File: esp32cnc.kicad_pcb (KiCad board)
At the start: 2 copper layers, 88.3 x 113.7 mm, 25 parts, among them J1 Barrel_Jack, J2 USB_B_Micro, J3 Micro_SD_Card_Det1, J4 Screw_Terminal_01x04, J5 Screw_Terminal_01x04, J6 Screw_Terminal_01x04, J7 Screw_Terminal_01x02, U1 ESP32-WROOM-32, U2 OKI-78SR-3.3_1.5-W36-C, U3 CH330N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

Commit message: Init
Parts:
- moved J1 0.71 mm to (121.9, 122.9)
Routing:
- net unconnected-(J2-Shield-Pad6)_4: track 0.00 -> 16.3 mm
- net GND: track 63.1 -> 74.9 mm, vias 8 -> 9
- net +3.3V: track 173.7 -> 181.3 mm, vias 4 -> 8
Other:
- board size 88.3 x 113.7 mm -> 91.4 x 116.8 mm

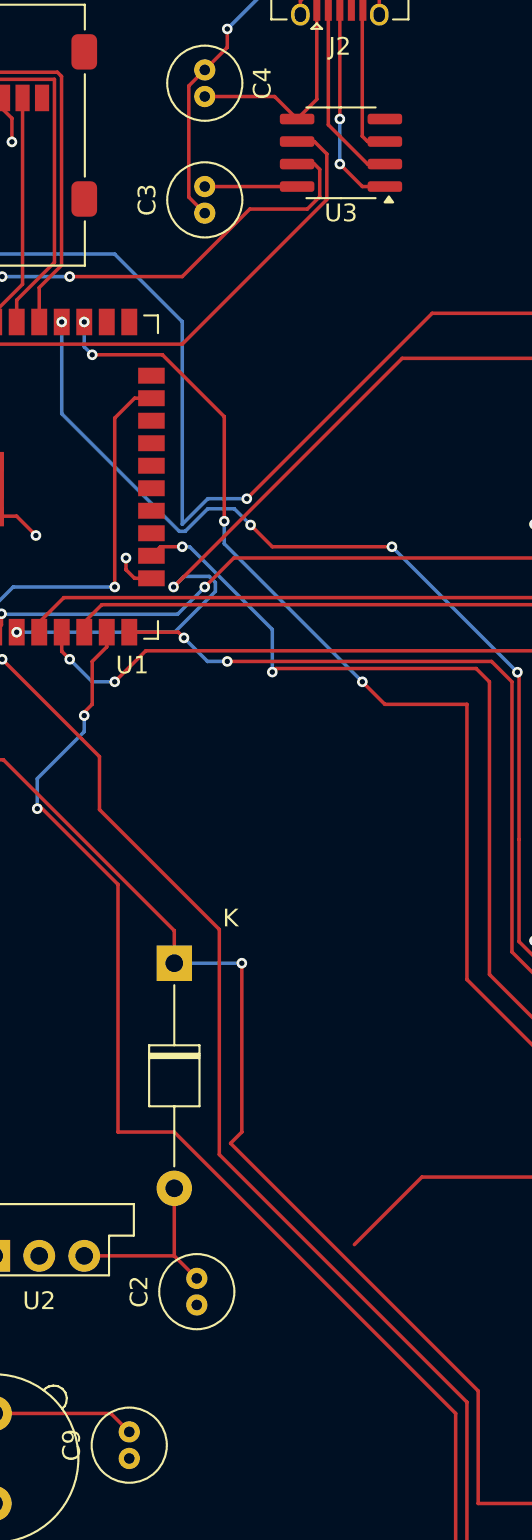
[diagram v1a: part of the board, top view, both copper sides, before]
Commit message: change to ch340n
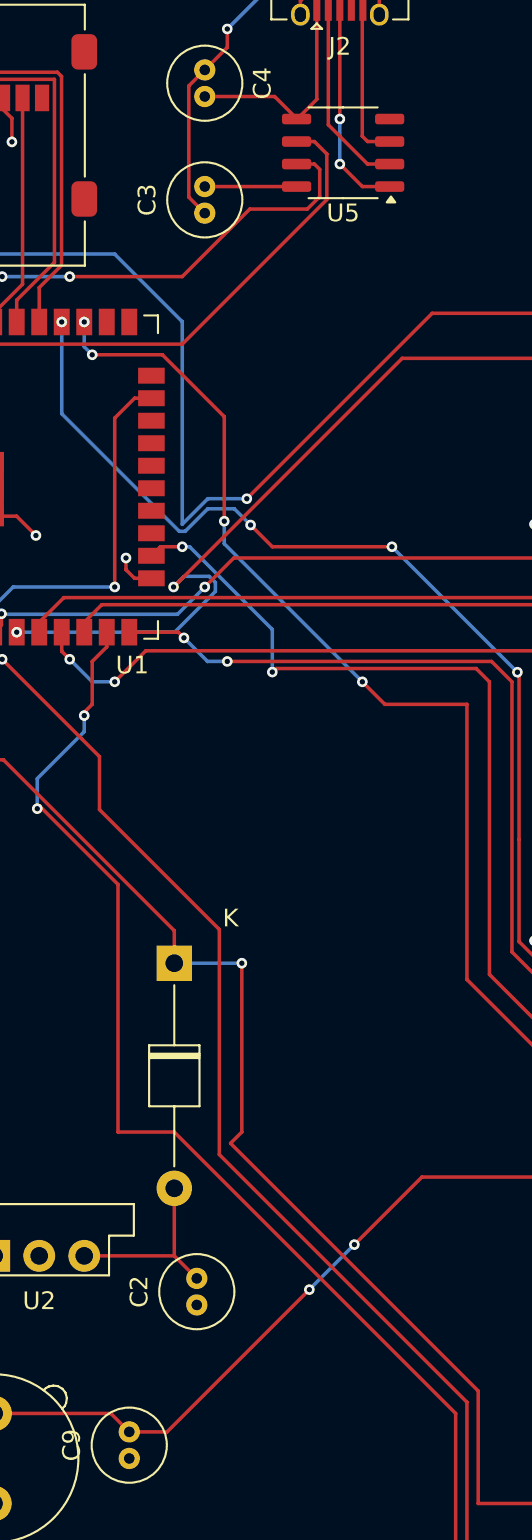
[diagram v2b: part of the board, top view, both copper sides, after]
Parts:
- removed U3: CH330N, Package_SO:SOIC-8_3.9x4.9mm_P1.27mm
- added U5: CH340N, Package_SO:SOP-8_3.9x4.9mm_P1.27mm, F.Cu at (141.6, 39.4)
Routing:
- net +12V: track 152.2 -> 169.2 mm, vias 6 -> 8

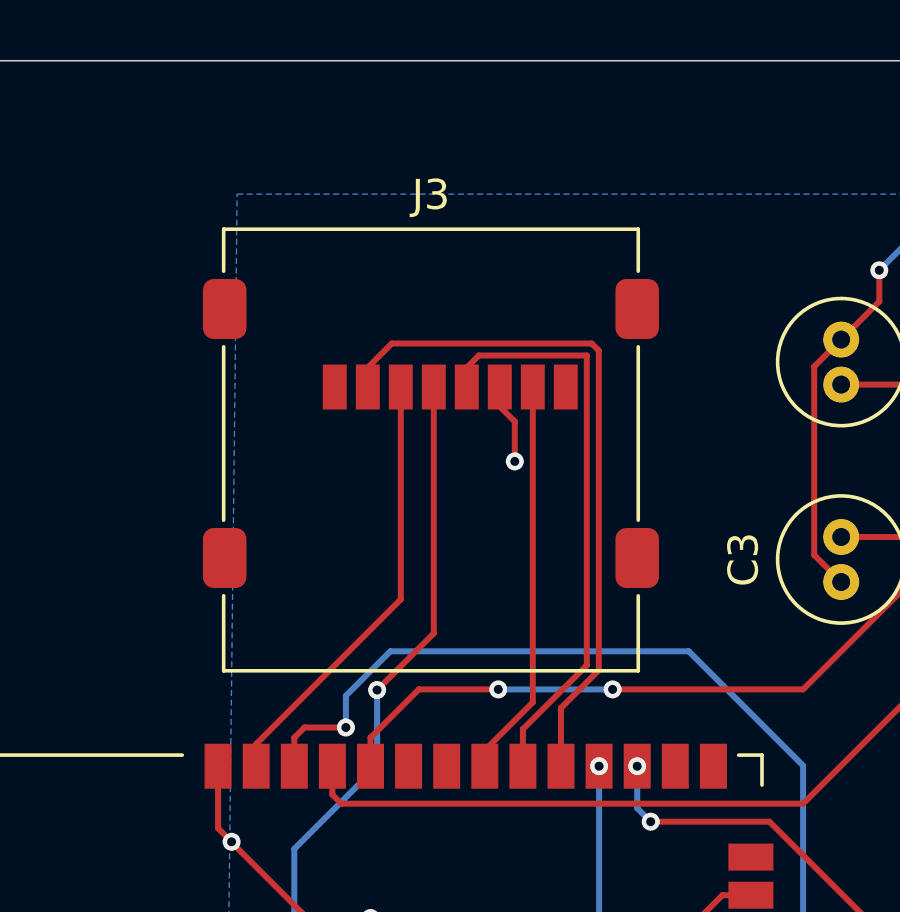
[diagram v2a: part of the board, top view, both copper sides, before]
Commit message: rotate SD-Card
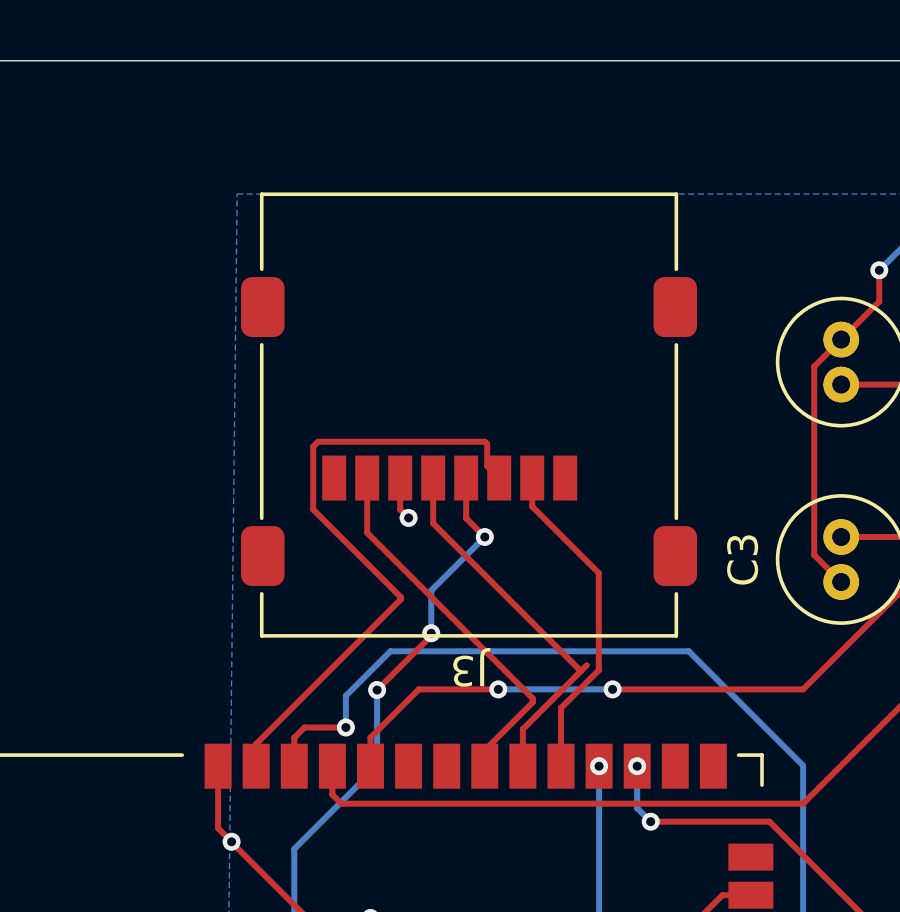
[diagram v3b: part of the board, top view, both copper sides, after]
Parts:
- moved J3 1.72 mm to (121.4, 37.2), turned to 180 degrees
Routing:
- net CS_SD: track 23.2 -> 11.0 mm
- net SCK: track 19.4 -> 12.7 mm
- net MOSI: track 14.6 -> 21.1 mm
- net +3.3V: track 181.3 -> 179.3 mm, vias 8 -> 10
- net GND: track 74.9 -> 73.6 mm
- net MISO: track 13.3 -> 12.6 mm

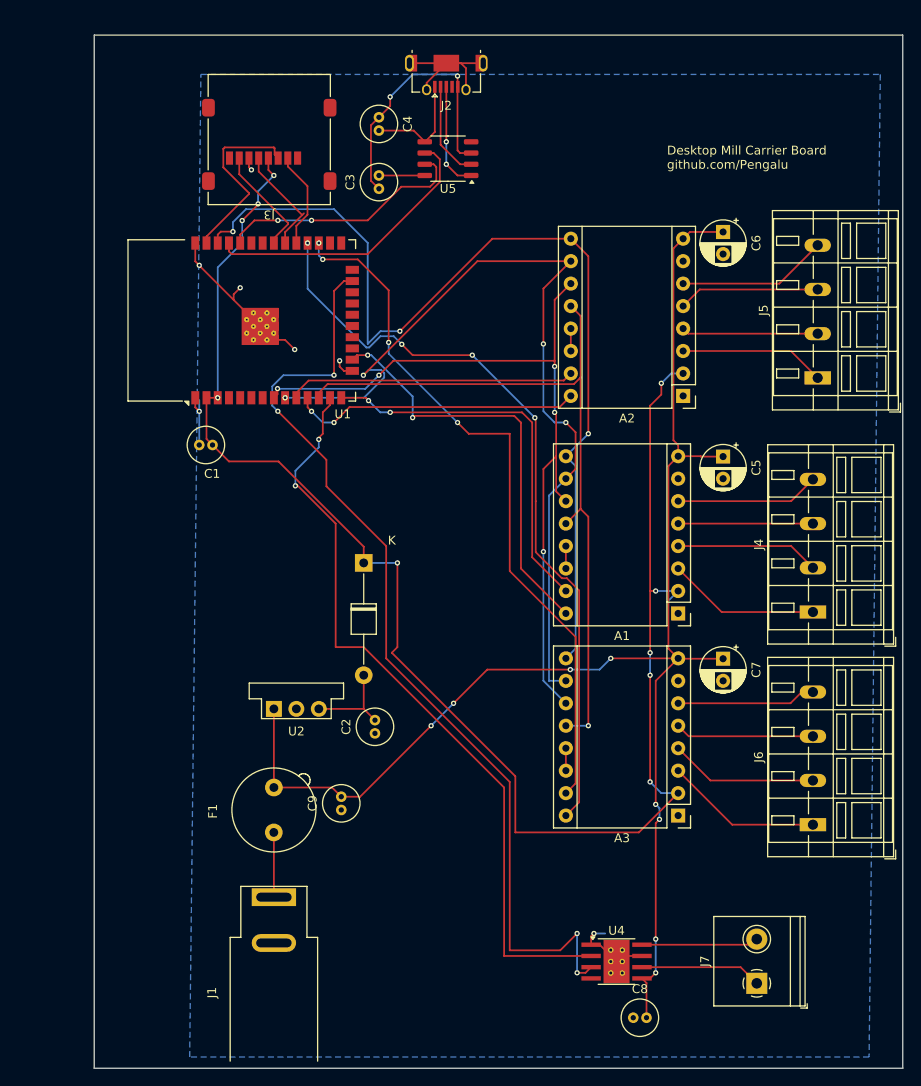
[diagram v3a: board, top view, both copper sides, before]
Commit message: flipped rx/tx, added boot button, added ILM resistor
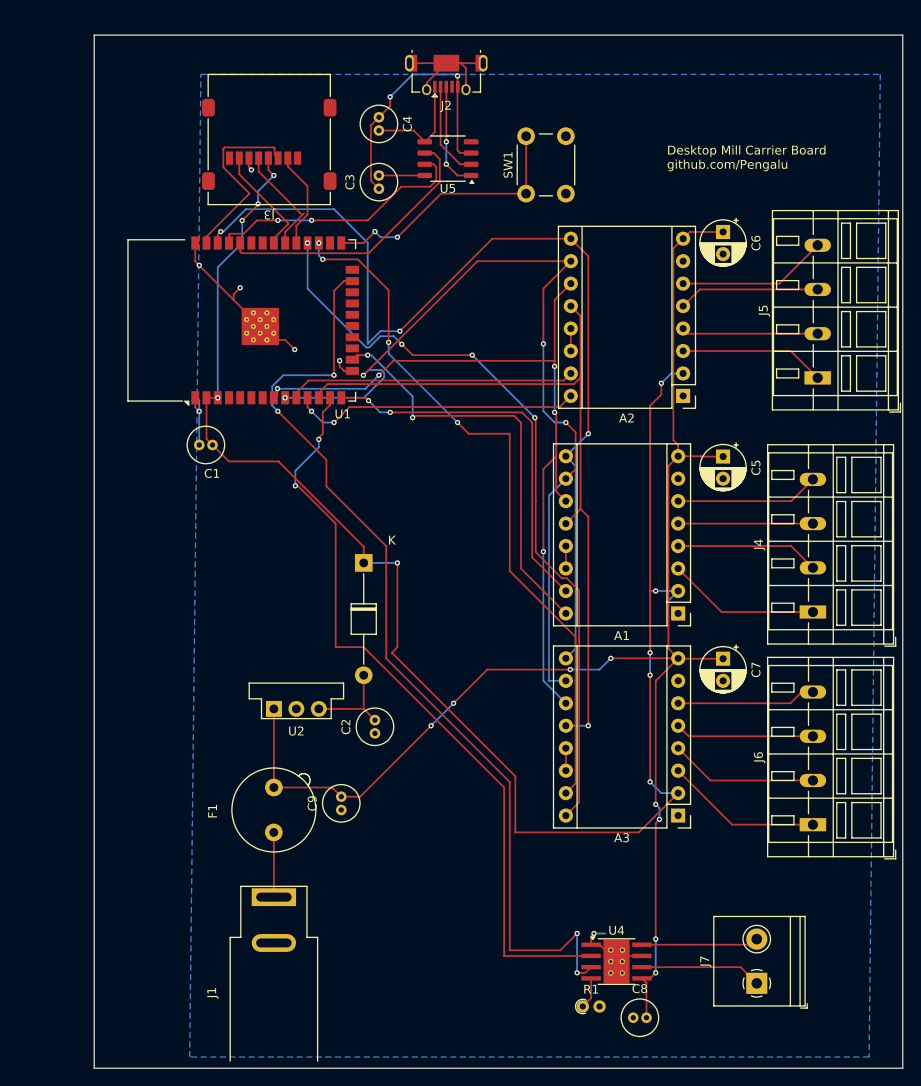
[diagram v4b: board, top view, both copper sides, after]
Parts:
- added R1: 18k, Resistor_THT:R_Axial_DIN0204_L3.6mm_D1.6mm_P1.90mm_Vertical, F.Cu at (156.8, 135.3)
- added SW1: SW_Push, Button_Switch_THT:SW_PUSH_6mm, F.Cu at (150.4, 43.3)
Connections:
- U1 pad 25: unconnected-(U1-IO0-Pad25) -> Net-(U1-IO0)
- U1 pad 34: RX -> TX
- U1 pad 35: TX -> RX
- U4 pad 4: unconnected-(U4-ILIM-Pad4) -> Net-(U4-ILIM)
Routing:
- net Net-(U1-IO0): track 0.00 -> 30.2 mm, vias 0 -> 2
- net Net-(U4-ILIM): track 0.00 -> 3.57 mm
- net RX: track 28.6 -> 29.9 mm
- net TX: track 32.8 -> 31.6 mm
- net MOTOR_EN: track 110.9 -> 110.3 mm
